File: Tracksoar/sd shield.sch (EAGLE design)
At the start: 10 parts, among them U2 HEX_CONVERTER

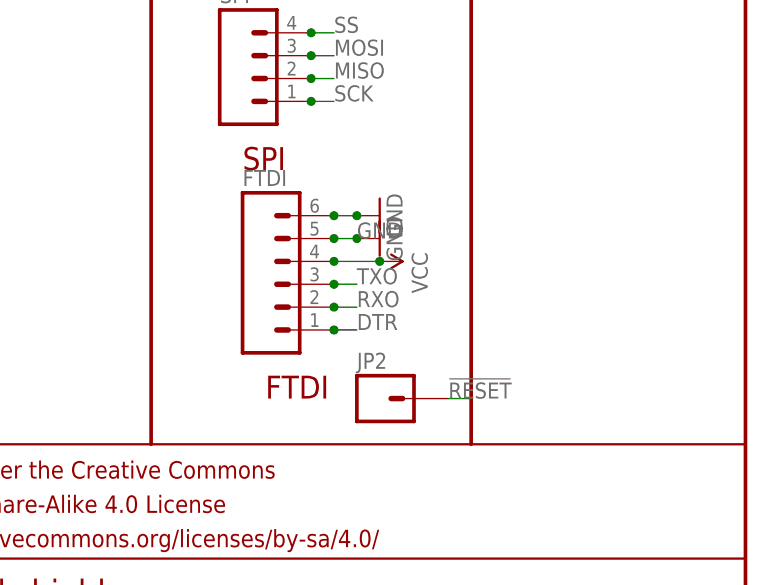
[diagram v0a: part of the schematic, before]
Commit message: replace headers
replaced 2.54mm headers on all production boards with 2mm headers to
resolve daughter board issues.
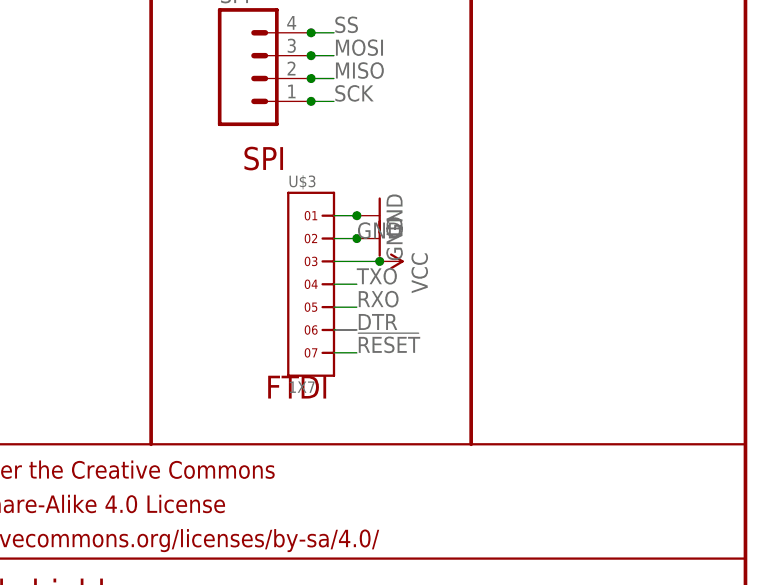
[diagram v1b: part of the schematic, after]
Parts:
- removed FTDI: (no value), SparkFun-Connectors:M06NO_SILK_FEMALE_PTH
- removed JP2: (no value), SparkFun-Connectors:M01PTH
- added U$3: 1X7, headers(2mm):1X7
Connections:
- net !RESET: now also U$3.7; no longer JP2.1
- net DTR: now also U$3.6; no longer FTDI.1
- net GND: now also U$3.1, U$3.2; no longer FTDI.5, FTDI.6
- net RXO: now also U$3.5; no longer FTDI.2
- net TXO: now also U$3.4; no longer FTDI.3
- net VCC: now also U$3.3; no longer FTDI.4
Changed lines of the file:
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@@
 </classes>
 <parts>
-<part name="FTDI" library="SparkFun-Connectors" deviceset="M06" device="NO_SILK_FEMALE_PTH"/>
 <part name="GND22" library="SparkFun-Aesthetics" deviceset="GND" device=""/>
 <part name="SUPPLY9" library="SparkFun-Aesthetics" deviceset="VCC" device=""/>
@@
 <part name="GND10" library="SparkFun-Aesthetics" deviceset="GND" device=""/>
 <part name="TX1" library="SparkFun-Connectors" deviceset="M02" device="JST-PTH-VERT" value="TX"/>
-<part name="JP2" library="SparkFun-Connectors" deviceset="M01" device="PTH"/>
 <part name="C1" library="SparkFun-Passives" deviceset="CAP" device="0805" value="10uf"/>
 <part name="C2" library="SparkFun-Passives" deviceset="CAP" device="0805" value=".1uf"/>
@@
 <part name="U2" library="SparkFun-DigitalIC" deviceset="HEX_CONVERTER" device=""/>
 <part name="U$2" library="adafruit" deviceset="MICROSD" device=""/>
+<part name="U$3" library="headers(2mm)" deviceset="1X7" device=""/>
 </parts>
 <sheets>
@@
 </plain>
 <instances>
-<instance part="FTDI" gate="G$1" x="198.12" y="53.34"/>
 <instance part="GND22" gate="1" x="208.28" y="60.96" rot="R90"/>
 <instance part="SUPPLY9" gate="G$1" x="208.28" y="55.88" rot="R270"/>
@@
 <instance part="GND10" gate="1" x="208.28" y="58.42" rot="R90"/>
 <instance part="TX1" gate="G$1" x="193.04" y="91.44"/>
-<instance part="JP2" gate="G$1" x="208.28" y="40.64"/>
 <instance part="C1" gate="G$1" x="50.8" y="93.98" rot="R180"/>
 <instance part="C2" gate="G$1" x="55.88" y="93.98" rot="R180"/>
@@
 <instance part="U2" gate="G$1" x="114.3" y="121.92"/>
 <instance part="U$2" gate="G$1" x="160.02" y="152.4"/>
+<instance part="U$3" gate="G$1" x="200.66" y="53.34"/>
 </instances>
 <busses>
@@
 <net name="GND" class="0">
 <segment>
-<pinref part="FTDI" gate="G$1" pin="6"/>
 <wire x1="203.2" y1="60.96" x2="205.74" y2="60.96" width="0.1524" layer="91"/>
 <pinref part="GND22" gate="1" pin="GND"/>
-<junction x="203.2" y="60.96"/>
 <junction x="205.74" y="60.96"/>
-</segment>
-<segment>
-<pinref part="FTDI" gate="G$1" pin="5"/>
+<pinref part="U$3" gate="G$1" pin="1"/>
+</segment>
+<segment>
 <wire x1="203.2" y1="58.42" x2="205.74" y2="58.42" width="0.1524" layer="91"/>
 <label x="205.74" y="58.42" size="1.778" layer="95"/>
-<junction x="203.2" y="58.42"/>
 <pinref part="GND10" gate="1" pin="GND"/>
 <junction x="205.74" y="58.42"/>
+<pinref part="U$3" gate="G$1" pin="2"/>
 </segment>
 <segment>
@@
 <net name="VCC" class="0">
 <segment>
-<pinref part="FTDI" gate="G$1" pin="4"/>
 <wire x1="203.2" y1="55.88" x2="208.28" y2="55.88" width="0.1524" layer="91"/>
 <pinref part="SUPPLY9" gate="G$1" pin="VCC"/>
-<junction x="203.2" y="55.88"/>
 <junction x="208.28" y="55.88"/>
+<pinref part="U$3" gate="G$1" pin="3"/>
 </segment>
 <segment>
@@
 <net name="DTR" class="0">
 <segment>
-<pinref part="FTDI" gate="G$1" pin="1"/>
 <wire x1="203.2" y1="48.26" x2="205.74" y2="48.26" width="0.1524" layer="91"/>
 <label x="205.74" y="48.26" size="1.778" layer="95"/>
-<junction x="203.2" y="48.26"/>
+<pinref part="U$3" gate="G$1" pin="6"/>
 </segment>
 </net>
 <net name="RXO" class="0">
 <segment>
-<pinref part="FTDI" gate="G$1" pin="2"/>
 <wire x1="203.2" y1="50.8" x2="205.74" y2="50.8" width="0.1524" layer="91"/>
 <label x="205.74" y="50.8" size="1.778" layer="95"/>
-<junction x="203.2" y="50.8"/>
+<pinref part="U$3" gate="G$1" pin="5"/>
 </segment>
 </net>
 <net name="TXO" class="0">
 <segment>
-<pinref part="FTDI" gate="G$1" pin="3"/>
 <wire x1="203.2" y1="53.34" x2="205.74" y2="53.34" width="0.1524" layer="91"/>
 <label x="205.74" y="53.34" size="1.778" layer="95"/>
-<junction x="203.2" y="53.34"/>
+<pinref part="U$3" gate="G$1" pin="4"/>
 </segment>
 </net>
@@
 <net name="!RESET" class="0">
 <segment>
-<pinref part="JP2" gate="G$1" pin="1"/>
-<wire x1="215.9" y1="40.64" x2="218.44" y2="40.64" width="0.1524" layer="91"/>
-<label x="215.9" y="40.64" size="1.778" layer="95"/>
-</segment>
-</net>
+<wire x1="203.2" y1="45.72" x2="205.74" y2="45.72" width="0.1524" layer="91"/>
+<label x="205.74" y="45.72" size="1.778" layer="95"/>
+<pinref part="U$3" gate="G$1" pin="7"/>
+</segment>
+</net>
